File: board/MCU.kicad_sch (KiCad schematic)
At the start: 3 parts, among them J1 RJ45_LED_Shielded, U1 Teensy4.1_DEV-16771

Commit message: Final 1
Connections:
- net LAS: now reaches U1.7 (RX2)
- net +5V: now reaches U1.VIN
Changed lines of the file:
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@@
+	(wire
+		(pts
+			(xy 60.96 78.74) (xy 66.04 78.74)
+		)
+		(stroke
+			(width 0)
+			(type default)
+		)
+	)
 	(wire
 		(pts
@@
 	(wire
 		(pts
+			(xy 60.96 54.61) (xy 66.04 54.61)
+		)
+		(stroke
+			(width 0)
+			(type default)
+		)
+	)
+	(wire
+		(pts
 			(xy 60.96 93.98) (xy 66.04 93.98)
 		)
@@
 		(pts
 			(xy 170.18 55.88) (xy 170.18 77.47)
+		)
+		(stroke
+			(width 0)
+			(type default)
+		)
+	)
+	(wire
+		(pts
+			(xy 66.04 54.61) (xy 66.04 58.42)
 		)
 		(stroke
@@
 		(shape input)
 		(at 59.69 119.38 180)
+		(effects
+			(font
+				(size 1.27 1.27)
+			)
+			(justify right)
+		)
+	)
+	(hierarchical_label "LAS"
+		(shape output)
+		(at 60.96 78.74 180)
 		(effects
 			(font
@@
 					(unit 1)
 				)
+			)
+		)
+	)
+	(symbol
+		(lib_id "power:+5V")
+		(at 60.96 54.61 0)
+		(unit 1)
+		(exclude_from_sim no)
+		(in_bom yes)
+		(on_board yes)
+		(dnp no)
+		(fields_autoplaced yes)
+		(property "Reference" "#PWR074"
+			(at 60.96 58.42 0)
+			(effects
+				(font
+					(size 1.27 1.27)
+				)
+				(hide yes)
+			)
+		)
+		(property "Value" "+5V"
+			(at 60.96 49.53 0)
+			(effects
+				(font
+					(size 1.27 1.27)
+				)
+			)
+		)
+		(property "Footprint" ""
+			(at 60.96 54.61 0)
+			(effects
+				(font
+					(size 1.27 1.27)
+				)
+				(hide yes)
+			)
+		)
+		(property "Datasheet" ""
+			(at 60.96 54.61 0)
+			(effects
+				(font
+					(size 1.27 1.27)
+				)
+				(hide yes)
+			)
+		)
+		(property "Description" "Power symbol creates a global label with name \"+5V\""
+			(at 60.96 54.61 0)
+			(effects
+				(font
+					(size 1.27 1.27)
+				)
+				(hide yes)
+			)
+		)
+		(pin "1"
+		)
+		(instances
+			(project ""
+				(path "/dc5110f0-fe48-48cb-9429-81f6eb467763/288a157d-b3ae-473c-9edc-77c2d2f56fa4"
+					(reference "#PWR074")
+					(unit 1)
+				)

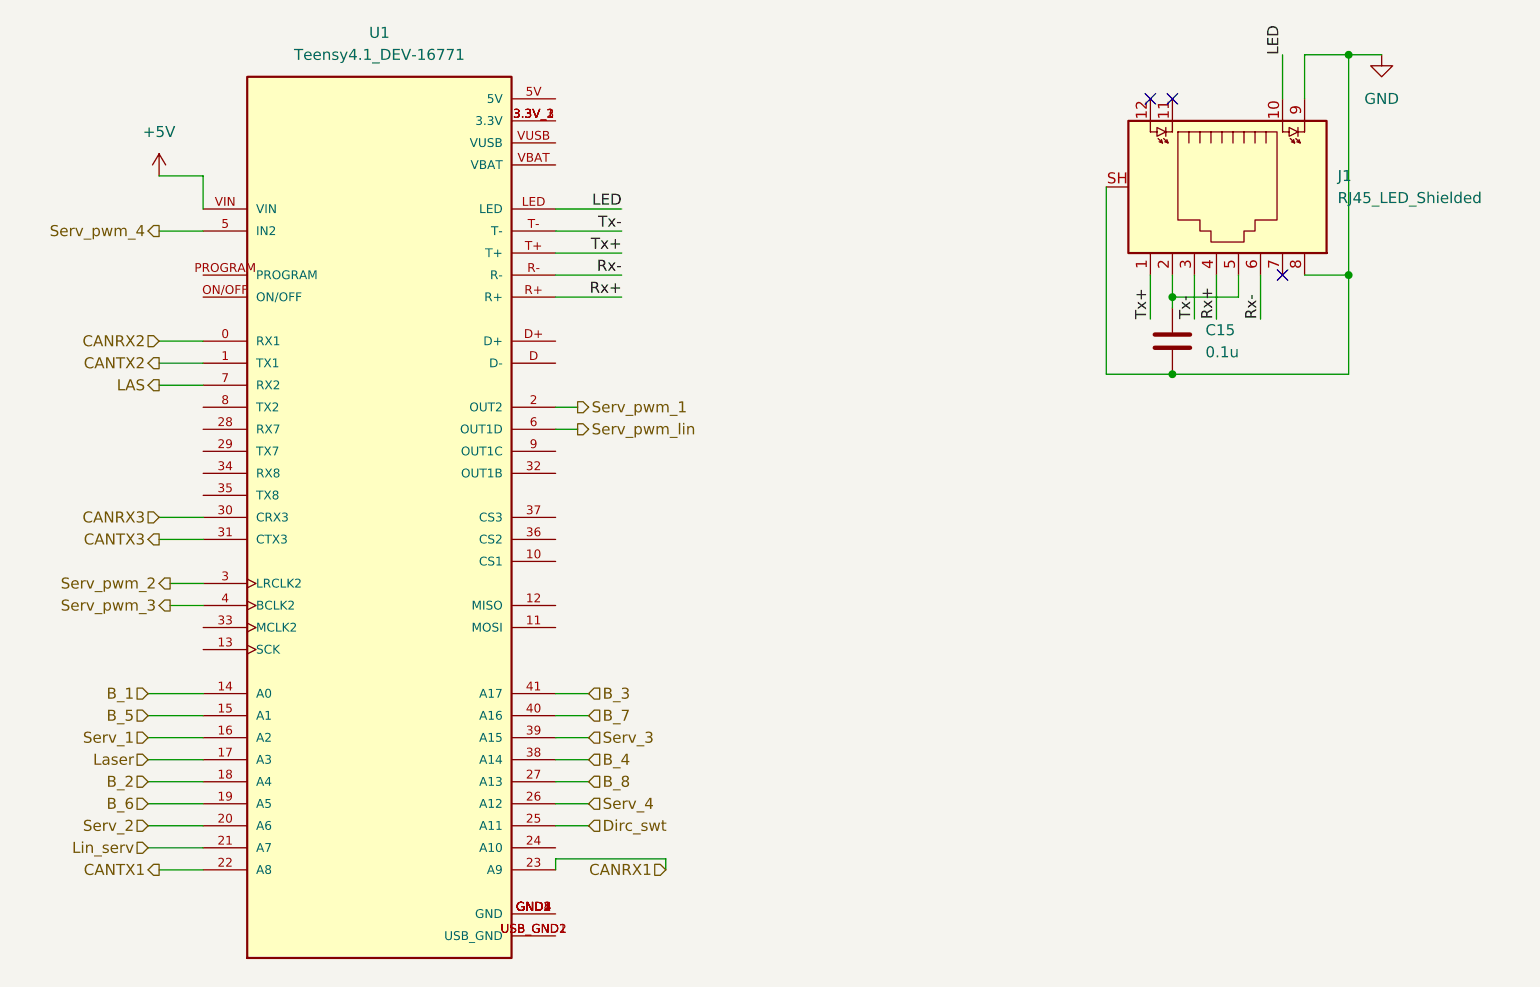
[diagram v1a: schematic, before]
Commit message: Fixed ground
fixed ground in MCU and added no connect flags.
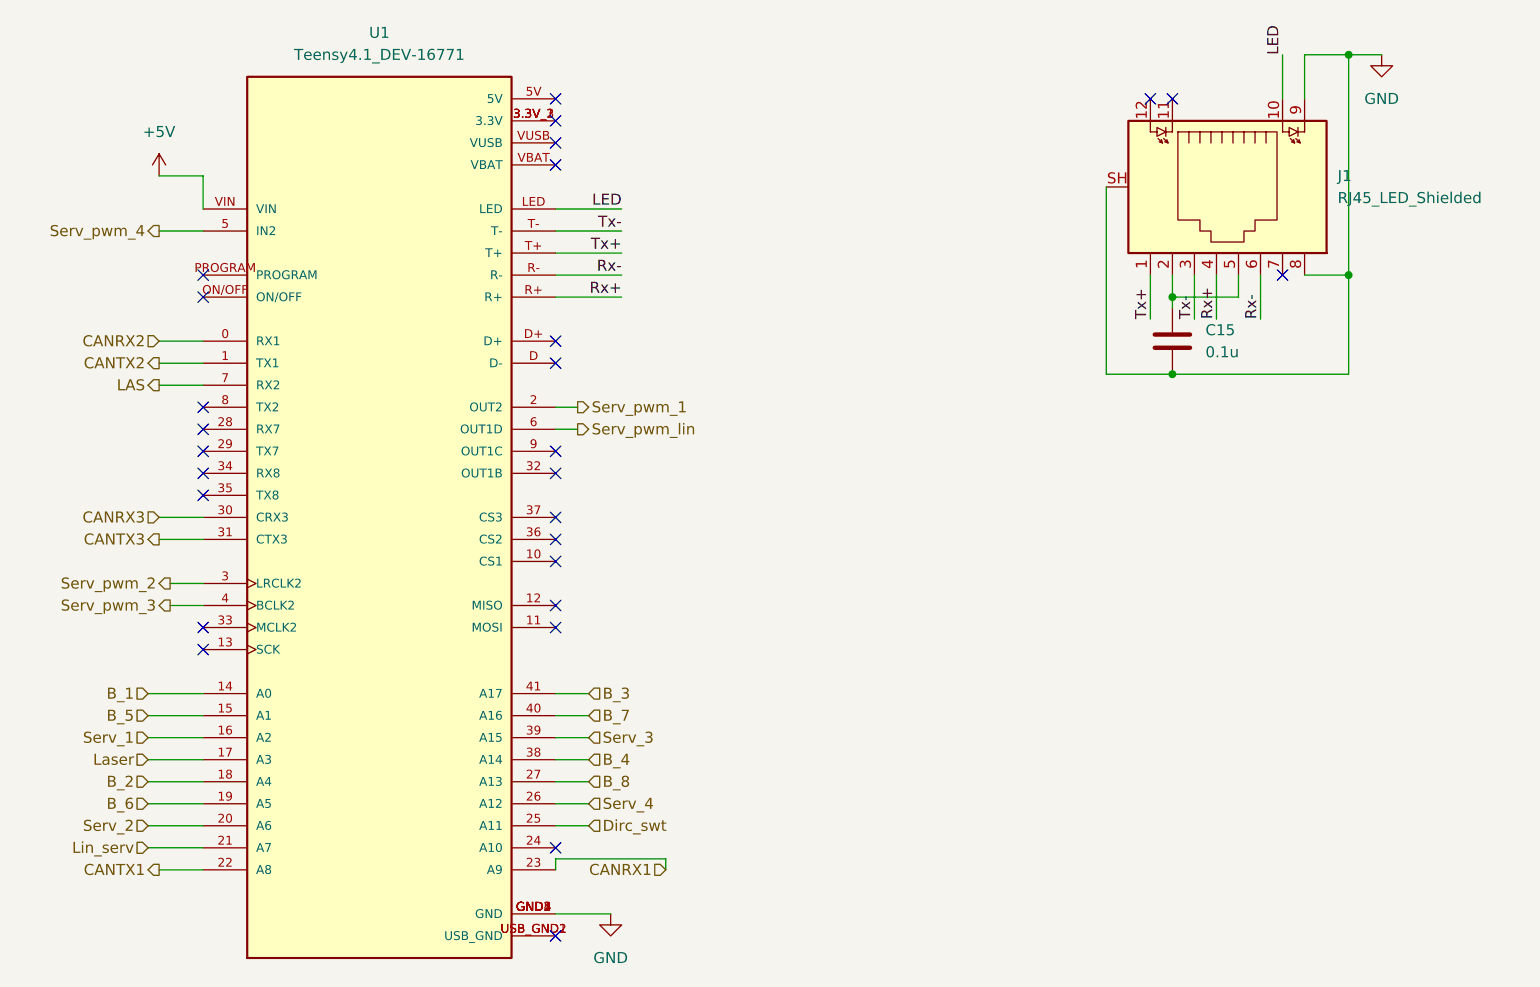
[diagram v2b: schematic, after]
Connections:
- net GND: now also U1.GND1 (GND), U1.GND2 (GND), U1.GND3 (GND), U1.GND4 (GND), U1.GND5 (GND)
- no-connect marks 3 -> 27
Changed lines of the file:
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@@
+	)
+	(no_connect
+		(at 106.68 73.66)
+	)
+	(no_connect
+		(at 106.68 132.08)
+	)
+	(no_connect
+		(at 106.68 99.06)
+	)
+	(no_connect
+		(at 106.68 104.14)
+	)
+	(no_connect
+		(at 106.68 96.52)
+	)
+	(no_connect
+		(at 66.04 88.9)
+	)
+	(no_connect
+		(at 106.68 76.2)
 	)
 	(no_connect
@@
 	)
 	(no_connect
+		(at 66.04 83.82)
+	)
+	(no_connect
 		(at 175.26 45.72)
 	)
 	(no_connect
+		(at 106.68 106.68)
+	)
+	(no_connect
+		(at 66.04 91.44)
+	)
+	(no_connect
+		(at 106.68 50.8)
+	)
+	(no_connect
+		(at 66.04 109.22)
+	)
+	(no_connect
+		(at 106.68 48.26)
+	)
+	(no_connect
+		(at 106.68 86.36)
+	)
+	(no_connect
+		(at 66.04 68.58)
+	)
+	(no_connect
+		(at 106.68 45.72)
+	)
+	(no_connect
+		(at 66.04 81.28)
+	)
+	(no_connect
+		(at 106.68 88.9)
+	)
+	(no_connect
+		(at 66.04 106.68)
+	)
+	(no_connect
 		(at 177.8 45.72)
 	)
+	(no_connect
+		(at 66.04 66.04)
+	)
+	(no_connect
+		(at 106.68 93.98)
+	)
+	(no_connect
+		(at 106.68 142.24)
+	)
+	(no_connect
+		(at 106.68 53.34)
+	)
+	(no_connect
+		(at 66.04 86.36)
+	)
 	(wire
 		(pts
@@
 		(pts
 			(xy 175.26 66.04) (xy 175.26 71.12)
+		)
+		(stroke
+			(width 0)
+			(type default)
+		)
+	)
+	(wire
+		(pts
+			(xy 106.68 139.7) (xy 113.03 139.7)
 		)
 		(stroke
@@
 					(unit 1)
 				)
+			)
+		)
+	)
+	(symbol
+		(lib_id "power:GND")
+		(at 113.03 139.7 0)
+		(unit 1)
+		(exclude_from_sim no)
+		(in_bom yes)
+		(on_board yes)
+		(dnp no)
+		(fields_autoplaced yes)
+		(property "Reference" "#PWR077"
+			(at 113.03 146.05 0)
+			(effects
+				(font
+					(size 1.27 1.27)
+				)
+				(hide yes)
+			)
+		)
+		(property "Value" "GND"
+			(at 113.03 144.78 0)
+			(effects
+				(font
+					(size 1.27 1.27)
+				)
+			)
+		)
+		(property "Footprint" ""
+			(at 113.03 139.7 0)
+			(effects
+				(font
+					(size 1.27 1.27)
+				)
+				(hide yes)
+			)
+		)
+		(property "Datasheet" ""
+			(at 113.03 139.7 0)
+			(effects
+				(font
+					(size 1.27 1.27)
+				)
+				(hide yes)
+			)
+		)
+		(property "Description" "Power symbol creates a global label with name \"GND\" , ground"
+			(at 113.03 139.7 0)
+			(effects
+				(font
+					(size 1.27 1.27)
+				)
+				(hide yes)
+			)
+		)
+		(pin "1"
+		)
+		(instances
+			(project ""
+				(path "/dc5110f0-fe48-48cb-9429-81f6eb467763/288a157d-b3ae-473c-9edc-77c2d2f56fa4"
+					(reference "#PWR077")
+					(unit 1)
+				)

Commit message: Schematic review changes
Updated molex connectors, can ics, buttons are no longer pull ups, and some appearence changes.
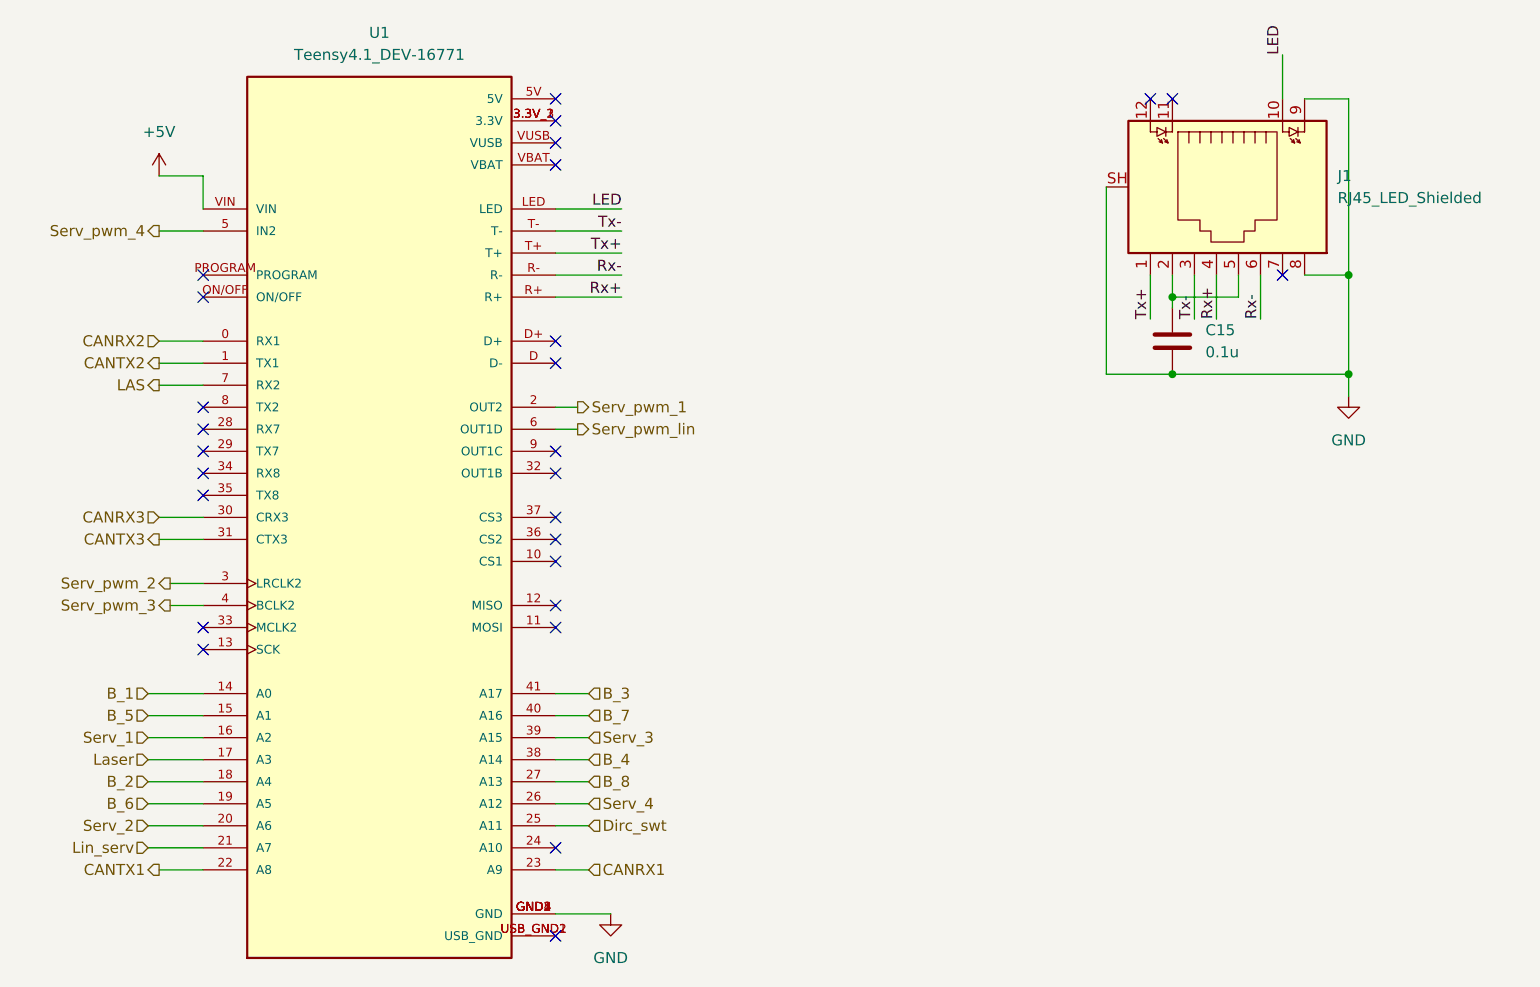
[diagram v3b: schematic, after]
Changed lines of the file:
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@@
 	)
 	(junction
-		(at 198.12 40.64)
+		(at 198.12 77.47)
 		(diameter 0)
 		(color 0 0 0 0)
@@
 	(wire
 		(pts
-			(xy 198.12 40.64) (xy 201.93 40.64)
-		)
-		(stroke
-			(width 0)
-			(type default)
-		)
-	)
-	(wire
-		(pts
 			(xy 60.96 78.74) (xy 66.04 78.74)
 		)
@@
 	(wire
 		(pts
-			(xy 106.68 133.35) (xy 106.68 134.62)
-		)
-		(stroke
-			(width 0)
-			(type default)
-		)
-	)
-	(wire
-		(pts
 			(xy 60.96 73.66) (xy 66.04 73.66)
 		)
@@
 	(wire
 		(pts
+			(xy 198.12 77.47) (xy 198.12 80.01)
+		)
+		(stroke
+			(width 0)
+			(type default)
+		)
+	)
+	(wire
+		(pts
 			(xy 60.96 134.62) (xy 66.04 134.62)
 		)
@@
 	(wire
 		(pts
-			(xy 198.12 66.04) (xy 198.12 40.64)
+			(xy 198.12 66.04) (xy 198.12 45.72)
 		)
 		(stroke
@@
 	(wire
 		(pts
-			(xy 193.04 40.64) (xy 198.12 40.64)
+			(xy 193.04 45.72) (xy 198.12 45.72)
 		)
 		(stroke
@@
 	(wire
 		(pts
-			(xy 119.38 133.35) (xy 106.68 133.35)
-		)
-		(stroke
-			(width 0)
-			(type default)
-		)
-	)
-	(wire
-		(pts
-			(xy 193.04 45.72) (xy 193.04 40.64)
+			(xy 110.49 134.62) (xy 106.68 134.62)
 		)
 		(stroke
@@
 		(pts
 			(xy 180.34 66.04) (xy 180.34 71.12)
-		)
-		(stroke
-			(width 0)
-			(type default)
-		)
-	)
-	(wire
-		(pts
-			(xy 119.38 134.62) (xy 119.38 133.35)
 		)
 		(stroke
@@
 	(hierarchical_label "CANRX1"
 		(shape input)
-		(at 119.38 134.62 180)
-		(effects
-			(font
-				(size 1.27 1.27)
-			)
-			(justify right)
+		(at 110.49 134.62 0)
+		(effects
+			(font
+				(size 1.27 1.27)
+			)
+			(justify left)
 		)
 	)
@@
 	(symbol
 		(lib_id "power:GND")
-		(at 201.93 40.64 0)
+		(at 198.12 80.01 0)
 		(unit 1)
 		(exclude_from_sim no)
@@
 		(fields_autoplaced yes)
 		(property "Reference" "#PWR036"
-			(at 201.93 46.99 0)
+			(at 198.12 86.36 0)
 			(effects
 				(font
@@
 		)
 		(property "Value" "GND"
-			(at 201.93 45.72 0)
+			(at 198.12 85.09 0)
 			(effects
 				(font
@@
 		)
 		(property "Footprint" ""
-			(at 201.93 40.64 0)
+			(at 198.12 80.01 0)
 			(effects
 				(font
@@
 		)
 		(property "Datasheet" ""
-			(at 201.93 40.64 0)
+			(at 198.12 80.01 0)
 			(effects
 				(font
@@
 		)
 		(property "Description" "Power symbol creates a global label with name \"GND\" , ground"
-			(at 201.93 40.64 0)
-			(effects
-				(font
+			(at 198.12 80.01 0)
+			(effects
+				(font

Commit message: Schematic review changes part 2 the electric boogaloo
finished fixing schematic. Made better names for heiracal pins. Made LED ressistors standard values.
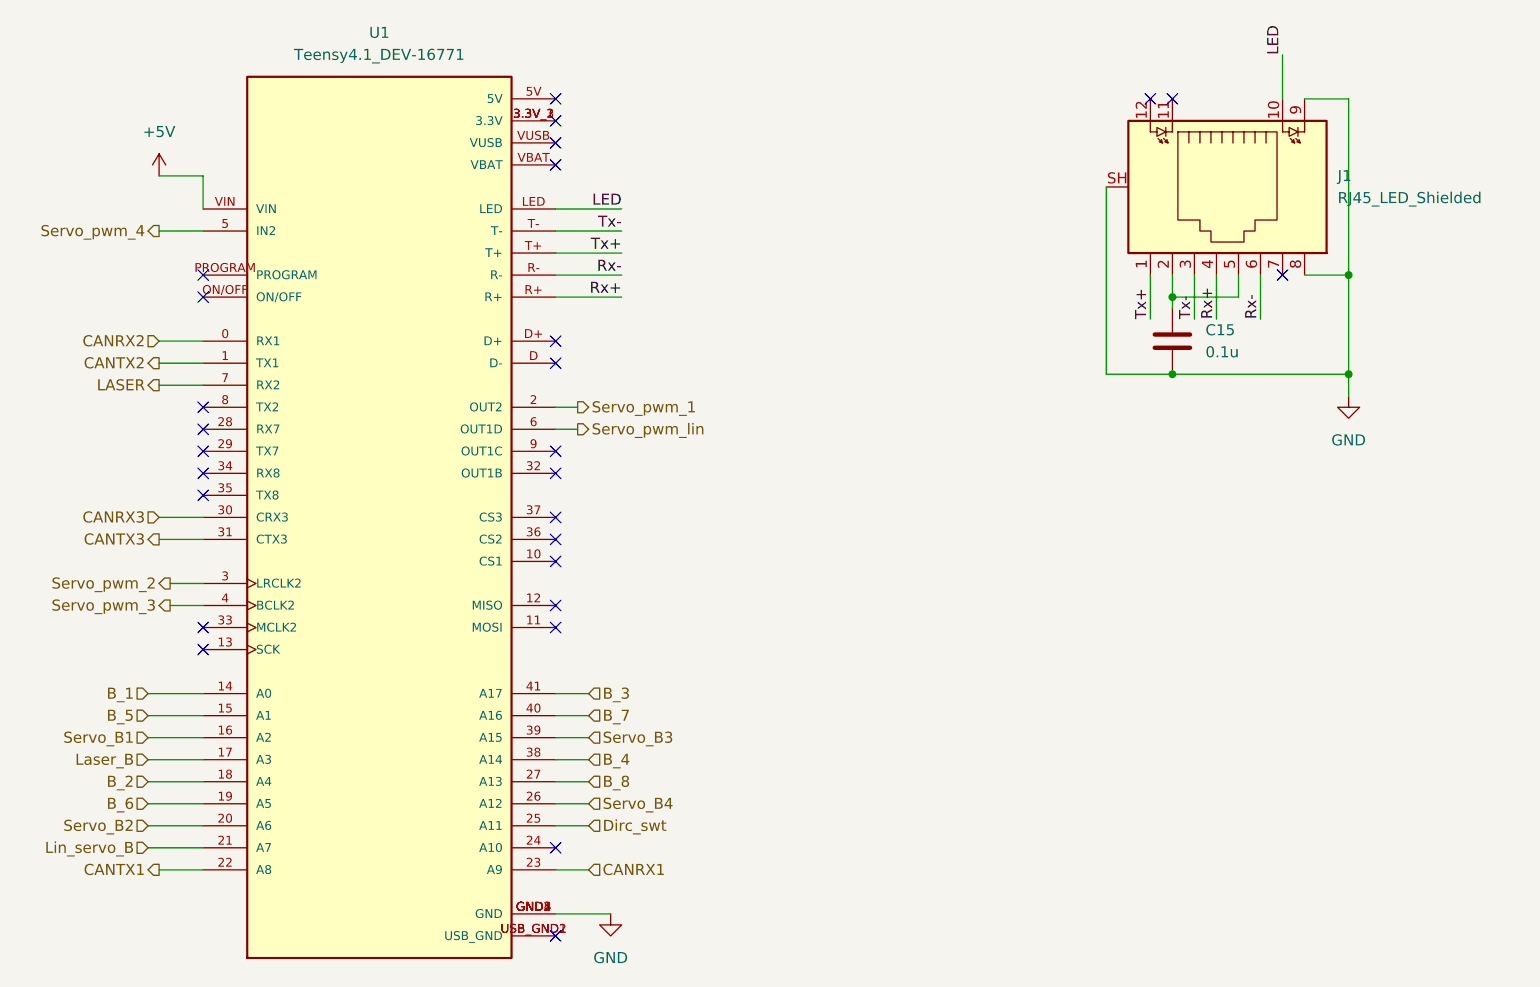
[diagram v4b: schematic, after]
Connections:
- net LAS renamed LASER
- net Laser renamed Laser_B
- net Lin_serv renamed Lin_servo_B
- net Serv_1 renamed Servo_B1
- net Serv_2 renamed Servo_B2
- net Serv_3 renamed Servo_B3
- net Serv_4 renamed Servo_B4
- net Serv_pwm_1 renamed Servo_pwm_1
- net Serv_pwm_2 renamed Servo_pwm_2
- net Serv_pwm_3 renamed Servo_pwm_3
- net Serv_pwm_4 renamed Servo_pwm_4
- net Serv_pwm_lin renamed Servo_pwm_lin
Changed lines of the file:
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@@
 		)
 	)
-	(hierarchical_label "Serv_4"
+	(hierarchical_label "Servo_B4"
 		(shape input)
 		(at 110.49 127 0)
@@
 		)
 	)
-	(hierarchical_label "Lin_serv"
+	(hierarchical_label "Lin_servo_B"
 		(shape input)
 		(at 59.69 132.08 180)
@@
 		)
 	)
-	(hierarchical_label "Serv_pwm_2"
+	(hierarchical_label "Servo_pwm_2"
 		(shape output)
 		(at 62.23 101.6 180)
@@
 		)
 	)
-	(hierarchical_label "Serv_pwm_1"
+	(hierarchical_label "Servo_pwm_1"
 		(shape output)
 		(at 109.22 81.28 0)
@@
 		)
 	)
-	(hierarchical_label "Serv_2"
+	(hierarchical_label "Servo_B2"
 		(shape input)
 		(at 59.69 129.54 180)
@@
 		)
 	)
-	(hierarchical_label "Serv_3"
+	(hierarchical_label "Servo_B3"
 		(shape input)
 		(at 110.49 119.38 0)
@@
 		)
 	)
-	(hierarchical_label "Serv_pwm_lin"
+	(hierarchical_label "Servo_pwm_lin"
 		(shape output)
 		(at 109.22 83.82 0)
@@
 		)
 	)
-	(hierarchical_label "Serv_1"
+	(hierarchical_label "Servo_B1"
 		(shape input)
 		(at 59.69 119.38 180)
@@
 		)
 	)
-	(hierarchical_label "LAS"
+	(hierarchical_label "LASER"
 		(shape output)
 		(at 60.96 78.74 180)
@@
 		)
 	)
-	(hierarchical_label "Laser"
+	(hierarchical_label "Laser_B"
 		(shape input)
 		(at 59.69 121.92 180)
@@
 		)
 	)
-	(hierarchical_label "Serv_pwm_4"
+	(hierarchical_label "Servo_pwm_4"
 		(shape output)
 		(at 60.96 60.96 180)
@@
 		)
 	)
-	(hierarchical_label "Serv_pwm_3"
+	(hierarchical_label "Servo_pwm_3"
 		(shape output)
 		(at 62.23 104.14 180)

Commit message: Prototype Layout
Made an initial Layout to be edited and changed uwu
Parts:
- C15: footprint (none) -> Capacitor_SMD:C_0603_1608Metric_Pad1.08x0.95mm_HandSolder
- J1: footprint (none) -> MRDT_Connectors:RJ45_Teensy
- U1: footprint MODULE_DEV-16771 -> MRDT_Shields:Teensy_4_1
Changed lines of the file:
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@@
 			)
 		)
-		(property "Footprint" "MODULE_DEV-16771"
+		(property "Footprint" "MRDT_Shields:Teensy_4_1"
 			(at 139.7 101.6 0)
 			(effects
@@
 			)
 		)
-		(property "Footprint" ""
+		(property "Footprint" "MRDT_Connectors:RJ45_Teensy"
 			(at 183.515 55.88 90)
 			(effects
@@
 			)
 		)
-		(property "Footprint" ""
+		(property "Footprint" "Capacitor_SMD:C_0603_1608Metric_Pad1.08x0.95mm_HandSolder"
 			(at 178.7652 77.47 0)
 			(effects
